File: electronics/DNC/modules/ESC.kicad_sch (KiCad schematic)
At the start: 20 parts

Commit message: Se reemplazó la hoja del IMU por la de sensores y se agregó la hoja de indicadores
- Nueva hoja Sensores: IMU BMI270 (SPI1) y barómetro BMP581 (I2C1 propio, jumper BARO_ADDR).
- Nueva hoja Indicadores: buzzer piezo CPT-12123 con FDV303N y LEDs de estado en PB4/PB5.
- Se eliminó la hoja IMU.
- MicroSD por SDIO de 4 bits con filtro TPD6F002 y TVS ESD5Z3.3 en VDD.
- PMS: AP2112K en 3V3_SYS y LP5907 + ferrita en 3V3_SEN.
- Motores movidos a PA0-PA3 (TIM5) para liberar el SDIO.
- Arquitectura.drawio actualizado a la arquitectura v1 (ELRS por UART, sin OLED).
- Se agregó docs/RESUMEN_PROYECTO_DNC.md con decisiones y pendientes.

Co-Authored-By: Claude Opus 5.5 <noreply@anthropic.com>
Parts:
- renumbered H6 to H?, H5 to H?, H4 to H?, H3 to H?, H1 to H?, H8 to H?, H2 to H?, H7 to H?
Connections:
- net MOTOR_1 renamed MTR1
- net MOTOR_2 renamed MTR2
- net MOTOR_3 renamed MTR3
- net MOTOR_4 renamed MTR4
- net VIN renamed VIN_MTR
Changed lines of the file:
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@@
 	(wire
 		(pts
-			(xy 116.84 78.74) (xy 121.92 78.74)
+			(xy 106.68 78.74) (xy 121.92 78.74)
 		)
 		(stroke
@@
 		)
 	)
-	(label "MOTOR_3"
+	(label "MTR3"
 		(at 119.38 121.92 0)
 		(effects
@@
 		)
 	)
-	(label "MOTOR_1"
+	(label "MTR1"
 		(at 119.38 111.76 0)
 		(effects
@@
 		)
 	)
-	(label "MOTOR_4"
+	(label "MTR4"
 		(at 119.38 127 0)
 		(effects
@@
 		)
 	)
-	(label "VIN"
-		(at 118.11 78.74 0)
+	(label "VIN_MTR"
+		(at 107.95 78.74 0)
 		(effects
 			(font
@@
 		)
 	)
-	(label "MOTOR_2"
+	(label "MTR2"
 		(at 119.4027 116.84 0)
 		(effects
@@
 		)
 	)
-	(hierarchical_label "VIN"
+	(hierarchical_label "VIN_MTR"
 		(shape input)
-		(at 116.84 78.74 180)
+		(at 106.68 78.74 180)
 		(effects
 			(font
@@
 		)
 	)
-	(hierarchical_label "MOTOR_1"
+	(hierarchical_label "MTR1"
 		(shape input)
 		(at 118.11 111.76 180)
@@
 		)
 	)
-	(hierarchical_label "MOTOR_3"
+	(hierarchical_label "MTR3"
 		(shape input)
 		(at 118.11 121.92 180)
@@
 		)
 	)
-	(hierarchical_label "MOTOR_4"
+	(hierarchical_label "MTR4"
 		(shape input)
 		(at 118.11 127 180)
@@
 		)
 	)
-	(hierarchical_label "MOTOR_2"
+	(hierarchical_label "MTR2"
 		(shape input)
 		(at 118.11 116.84 180)
@@
 		(dnp no)
 		(fields_autoplaced yes)
-		(property "Reference" "H6"
+		(property "Reference" "H?"
 			(at 161.29 137.1599 90)
 			(show_name no)
@@
 			(project "DNC"
 				(path "/abee636e-ad3a-4ba4-b95f-d0cf4a6d3d85/18620967-b01e-4bf5-b906-54a6ad8f63f3"
-					(reference "H6")
+					(reference "H?")
 					(unit 1)
 				)
@@
 		(dnp no)
 		(fields_autoplaced yes)
-		(property "Reference" "H5"
+		(property "Reference" "H?"
 			(at 161.29 132.0799 90)
 			(show_name no)
@@
 			(project "DNC"
 				(path "/abee636e-ad3a-4ba4-b95f-d0cf4a6d3d85/18620967-b01e-4bf5-b906-54a6ad8f63f3"
-					(reference "H5")
+					(reference "H?")
 					(unit 1)
 				)
@@
 		(dnp no)
 		(fields_autoplaced yes)
-		(property "Reference" "H4"
+		(property "Reference" "H?"
 			(at 161.29 125.7299 90)
 			(show_name no)
@@
 			(project "DNC"
 				(path "/abee636e-ad3a-4ba4-b95f-d0cf4a6d3d85/18620967-b01e-4bf5-b906-54a6ad8f63f3"
-					(reference "H4")
+					(reference "H?")
 					(unit 1)
 				)
@@
 		(dnp no)
 		(fields_autoplaced yes)
-		(property "Reference" "H3"
+		(property "Reference" "H?"
 			(at 161.29 120.6499 90)
 			(show_name no)
@@
 			(project "DNC"
 				(path "/abee636e-ad3a-4ba4-b95f-d0cf4a6d3d85/18620967-b01e-4bf5-b906-54a6ad8f63f3"
-					(reference "H3")
+					(reference "H?")
 					(unit 1)
 				)
@@
 		(dnp no)
 		(fields_autoplaced yes)
-		(property "Reference" "H1"
+		(property "Reference" "H?"
 			(at 161.29 110.4899 90)
 			(show_name no)
@@
 			(project "DNC"
 				(path "/abee636e-ad3a-4ba4-b95f-d0cf4a6d3d85/18620967-b01e-4bf5-b906-54a6ad8f63f3"
-					(reference "H1")
+					(reference "H?")
 					(unit 1)
 				)
@@
 		(dnp no)
 		(fields_autoplaced yes)
-		(property "Reference" "H8"
+		(property "Reference" "H?"
 			(at 161.29 147.3199 90)
 			(show_name no)
@@
 			(project "DNC"
 				(path "/abee636e-ad3a-4ba4-b95f-d0cf4a6d3d85/18620967-b01e-4bf5-b906-54a6ad8f63f3"
-					(reference "H8")
+					(reference "H?")
 					(unit 1)
 				)
@@
 		(dnp no)
 		(fields_autoplaced yes)
-		(property "Reference" "H2"
+		(property "Reference" "H?"
 			(at 161.29 115.5699 90)
 			(show_name no)
@@
 			(project "DNC"
 				(path "/abee636e-ad3a-4ba4-b95f-d0cf4a6d3d85/18620967-b01e-4bf5-b906-54a6ad8f63f3"
-					(reference "H2")
+					(reference "H?")
 					(unit 1)
 				)
@@
 		(in_pos_files yes)
 		(dnp no)
-		(property "Reference" "#PWR04"
+		(property "Reference" "#PWR?"
 			(at 151.13 158.75 0)
 			(hide yes)
@@
 			(project "DNC"
 				(path "/abee636e-ad3a-4ba4-b95f-d0cf4a6d3d85/18620967-b01e-4bf5-b906-54a6ad8f63f3"
-					(reference "#PWR04")
+					(reference "#PWR?")
 					(unit 1)
 				)
@@
 		(dnp no)
 		(fields_autoplaced yes)
-		(property "Reference" "H7"
+		(property "Reference" "H?"
 			(at 161.29 142.2399 90)
 			(show_name no)
@@
 			(project "DNC"
 				(path "/abee636e-ad3a-4ba4-b95f-d0cf4a6d3d85/18620967-b01e-4bf5-b906-54a6ad8f63f3"
-					(reference "H7")
+					(reference "H?")
 					(unit 1)
 				)

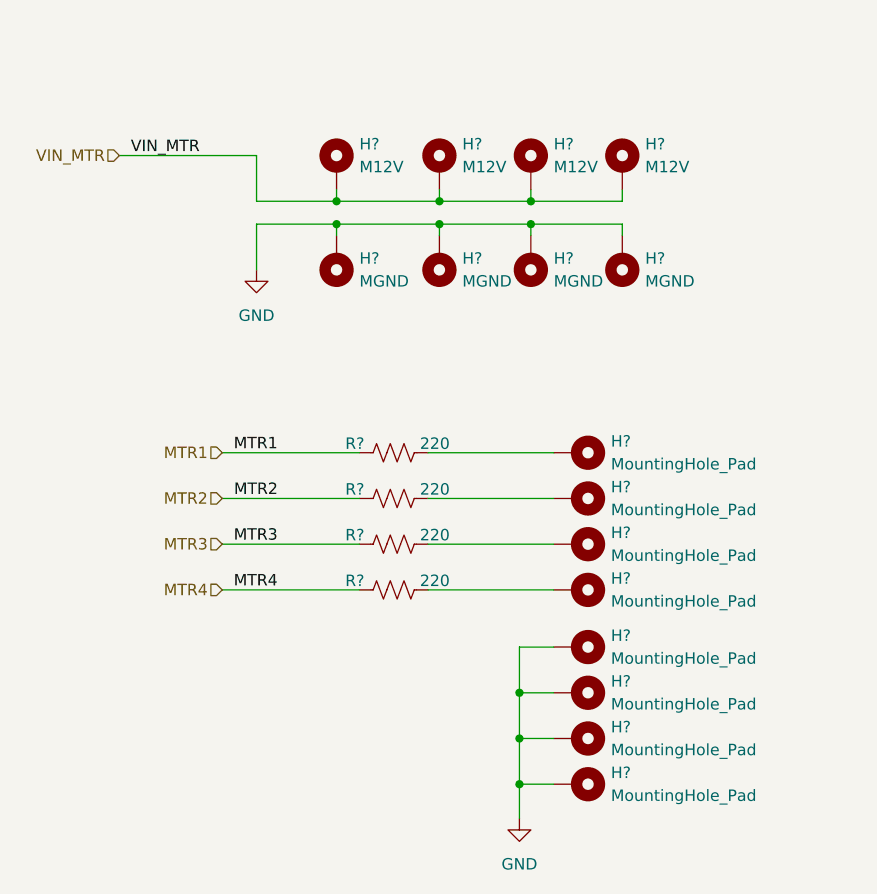
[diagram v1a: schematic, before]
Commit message: Hoja ESC: pads de potencia THT, ESD en las señales MTR y pads de señal/GND
- Por ESC: M12V (VIN_MTR) y MGND (GND) como Conn_01x01 con huella
  Connector_Wire:SolderWire-1.5sqmm_1x01_D1.7mm_OD3.9mm (cable de 16 AWG, ~15 A por ESC en el MVP1);
  señal (MTRx_PAD, tras 220 ohm) y su tierra de referencia (GNDx_PAD) con TestPoint_Pad_2.0x2.0mm.
- ESD IEC 61000-4-2 nivel 4: USBLC6-4SC6 en los 4 pads de señal, VBUS a 3V3_SYS con 100 nF.
- Se eliminan los MountingHole_Pad y la dependencia de Gen_devices en esta hoja.
- Raíz: solo reacomodos gráficos (netlist sin cambios).
- Los huecos de montaje se agregan con el contorno de la placa.

Co-Authored-By: Claude Opus 5.5 <noreply@anthropic.com>
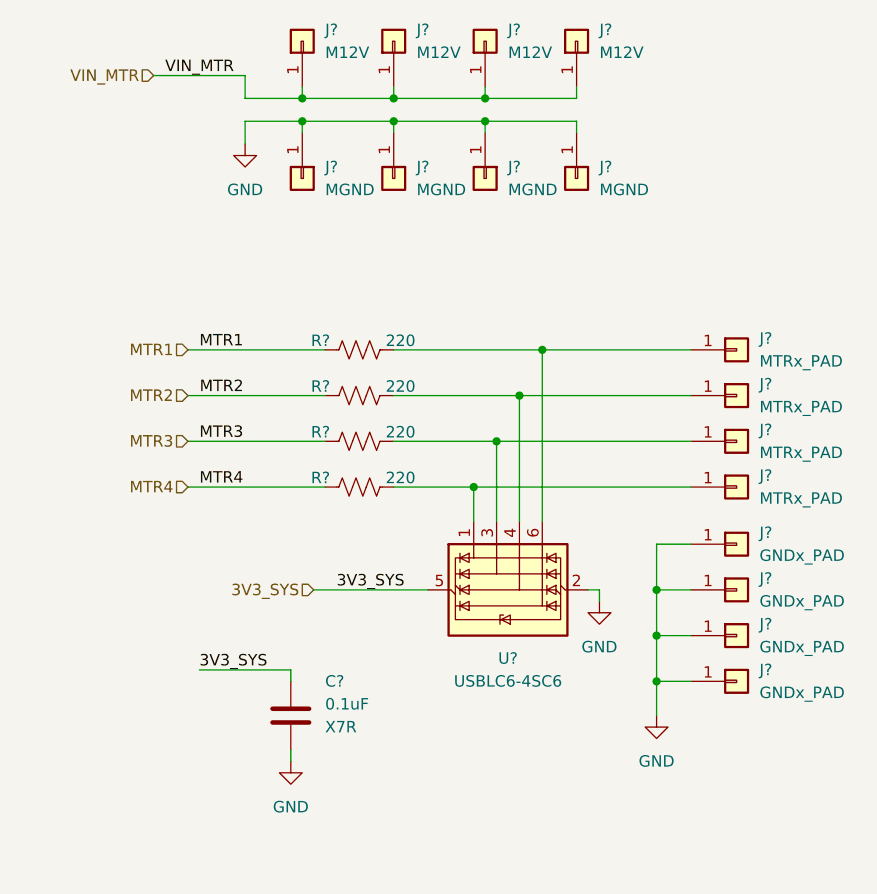
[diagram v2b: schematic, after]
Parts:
- removed H? (x4): MGND, Gen_devices:MountingHole_3.5mm_5.5mm, symbol Mechanical:MountingHole_Pad
- removed H? (x4): M12V, Gen_devices:MountingHole_3.5mm_5.5mm, symbol Mechanical:MountingHole_Pad
- removed H? (x8): MountingHole_Pad, symbol Mechanical:MountingHole_Pad
- added C?: 0.1uF, symbol Device:C
- added J? (x4): M12V, Connector_Wire:SolderWire-1.5sqmm_1x01_D1.7mm_OD3.9mm, symbol Connector_Generic:Conn_01x01
- added J? (x4): MGND, Connector_Wire:SolderWire-1.5sqmm_1x01_D1.7mm_OD3.9mm, symbol Connector_Generic:Conn_01x01
- added J? (x4): GNDx_PAD, TestPoint:TestPoint_Pad_2.0x2.0mm, symbol Connector_Generic:Conn_01x01
- added J? (x4): MTRx_PAD, TestPoint:TestPoint_Pad_2.0x2.0mm, symbol Connector_Generic:Conn_01x01
- added U?: USBLC6-4SC6, Package_TO_SOT_SMD:SOT-23-6, symbol Power_Protection:USBLC6-4SC6
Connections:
- net GND: now also C?.2, J?.1 (Pin_1), J?.1 (Pin_1), J?.1 (Pin_1), J?.1 (Pin_1), J?.1 (Pin_1), J?.1 (Pin_1), J?.1 (Pin_1), J?.1 (Pin_1), U?.2 (GND)
- net VIN_MTR: now also J?.1 (Pin_1), J?.1 (Pin_1), J?.1 (Pin_1), J?.1 (Pin_1)
- net at R?.2: now also J?.1 (Pin_1), U?.6 (I/O4)
- net at R?.2: now also J?.1 (Pin_1), U?.1 (I/O1)
- net at R?.2: now also J?.1 (Pin_1), U?.3 (I/O2)
- net at R?.2: now also J?.1 (Pin_1), U?.4 (I/O3)
- new net 3V3_SYS: C?.1, U?.5 (VBUS)
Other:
- moved on the sheet: R?
